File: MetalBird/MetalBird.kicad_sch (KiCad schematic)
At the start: 63 parts, among them J1 Battery Conn, J10 VTX Conn, J2 SWD, J3 ESC1, J4 ESC2, J5 ESC3, J6 ESC4, J7 ELRS Reciver, J8 USB/UART DEBUG, J9 Camera Conn, Q1 PMOS, SW1 SW_Push_Open, U1 STM32F411CEUx, U2 AMS1117-3.3, U3 MPU-6050, U4 BMP280, Y1 8MHz

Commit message: Assign Footprints to components
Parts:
- C1, C10, C11, C12, C13, C15, C16, C17, C18, C1A1, C20, C21, C22, C23, C25, C3, C4, C5, C6, C7, C8, C9: footprint (none) -> Capacitor_SMD:C_0603_1608Metric
- C14, C19, C2, C2A1: footprint (none) -> Capacitor_SMD:C_1206_3216Metric
- C24: footprint (none) -> Capacitor_THT:CP_Radial_D6.3mm_P2.50mm
- D1, D2: footprint (none) -> LED_SMD:LED_0603_1608Metric
- J1, J10, J3, J4, J5, J6, J9: footprint (none) -> Connector_PinHeader_2.54mm:PinHeader_1x03_P2.54mm_Vertical
- J2, J7, J8: footprint (none) -> Connector_PinHeader_2.54mm:PinHeader_1x04_P2.54mm_Vertical
- MP2331H1: footprint (none) -> Package_TO_SOT_SMD:SOT-583-8
- Q1: footprint (none) -> Package_TO_SOT_SMD:SOT-23
- R1, R11, R12, R13, R14, R15, R16, R17, R2, R3, R4, R5, R6, R7, R8: footprint (none) -> Resistor_SMD:R_0603_1608Metric
- SW1: footprint (none) -> Button_Switch_SMD:SW_SPST_PTS645Sx43SMTR92
- Y1: footprint (none) -> Crystal:Crystal_SMD_3225-4Pin_3.2x2.5mm
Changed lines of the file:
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@@
 			)
 		)
-		(property "Footprint" ""
+		(property "Footprint" "Capacitor_SMD:C_1206_3216Metric"
 			(at 37.1348 166.37 0)
 			(effects
@@
 			)
 		)
-		(property "Footprint" ""
+		(property "Footprint" "Capacitor_SMD:C_0603_1608Metric"
 			(at 132.3848 129.54 0)
 			(effects
@@
 			)
 		)
-		(property "Footprint" ""
+		(property "Footprint" "LED_SMD:LED_0603_1608Metric"
 			(at 113.03 110.49 0)
 			(effects
@@
 			)
 		)
-		(property "Footprint" ""
+		(property "Footprint" "Capacitor_SMD:C_0603_1608Metric"
 			(at 160.02 44.1452 0)
 			(effects
@@
 			)
 		)
-		(property "Footprint" ""
+		(property "Footprint" "Connector_PinHeader_2.54mm:PinHeader_1x04_P2.54mm_Vertical"
 			(at 43.18 85.09 0)
 			(effects
@@
 			)
 		)
-		(property "Footprint" ""
+		(property "Footprint" "Capacitor_SMD:C_0603_1608Metric"
 			(at 49.8348 166.37 0)
 			(effects
@@
 			)
 		)
-		(property "Footprint" ""
+		(property "Footprint" "Capacitor_SMD:C_0603_1608Metric"
 			(at 100.0252 40.64 0)
 			(effects
@@
 			)
 		)
-		(property "Footprint" ""
+		(property "Footprint" "Resistor_SMD:R_0603_1608Metric"
 			(at 87.63 171.958 90)
 			(effects
@@
 			)
 		)
-		(property "Footprint" ""
+		(property "Footprint" "Crystal:Crystal_SMD_3225-4Pin_3.2x2.5mm"
 			(at 124.46 63.5 0)
 			(effects
@@
 			)
 		)
-		(property "Footprint" ""
+		(property "Footprint" "Capacitor_SMD:C_1206_3216Metric"
 			(at 134.3152 179.07 0)
 			(effects
@@
 			)
 		)
-		(property "Footprint" ""
+		(property "Footprint" "Connector_PinHeader_2.54mm:PinHeader_1x03_P2.54mm_Vertical"
 			(at 212.09 80.01 0)
 			(effects
@@
 			)
 		)
-		(property "Footprint" ""
+		(property "Footprint" "Capacitor_SMD:C_0603_1608Metric"
 			(at 114.3 73.3552 0)
 			(effects
@@
 			)
 		)
-		(property "Footprint" ""
+		(property "Footprint" "Connector_PinHeader_2.54mm:PinHeader_1x03_P2.54mm_Vertical"
 			(at 43.18 44.45 0)
 			(effects
@@
 			)
 		)
-		(property "Footprint" ""
+		(property "Footprint" "Resistor_SMD:R_0603_1608Metric"
 			(at 120.65 112.268 90)
 			(effects
@@
 			)
 		)
-		(property "Footprint" ""
+		(property "Footprint" "Capacitor_SMD:C_0603_1608Metric"
 			(at 65.0748 151.13 0)
 			(effects
@@
 			)
 		)
-		(property "Footprint" ""
+		(property "Footprint" "Capacitor_SMD:C_0603_1608Metric"
 			(at 111.76 146.3548 0)
 			(effects
@@
 			)
 		)
-		(property "Footprint" ""
+		(property "Footprint" "Resistor_SMD:R_0603_1608Metric"
 			(at 29.972 41.91 90)
 			(effects
@@
 			)
 		)
-		(property "Footprint" ""
+		(property "Footprint" "Connector_PinHeader_2.54mm:PinHeader_1x03_P2.54mm_Vertical"
 			(at 212.09 95.25 0)
 			(effects
@@
 			)
 		)
-		(property "Footprint" ""
+		(property "Footprint" "Capacitor_SMD:C_0603_1608Metric"
 			(at 195.2752 62.23 0)
 			(effects
@@
 			)
 		)
-		(property "Footprint" ""
+		(property "Footprint" "Capacitor_SMD:C_0603_1608Metric"
 			(at 294.64 89.2048 0)
 			(effects
@@
 			)
 		)
-		(property "Footprint" ""
+		(property "Footprint" "Capacitor_SMD:C_0603_1608Metric"
 			(at 122.8852 40.64 0)
 			(effects
@@
 			)
 		)
-		(property "Footprint" ""
+		(property "Footprint" "Package_TO_SOT_SMD:SOT-23"
 			(at 29.21 26.67 0)
 			(effects
@@
 			)
 		)
-		(property "Footprint" ""
+		(property "Footprint" "Capacitor_SMD:C_0603_1608Metric"
 			(at 274.6248 139.7 0)
 			(effects
@@
 			)
 		)
-		(property "Footprint" ""
+		(property "Footprint" "LED_SMD:LED_0603_1608Metric"
 			(at 113.03 116.84 0)
 			(effects
@@
 			)
 		)
-		(property "Footprint" ""
+		(property "Footprint" "Connector_PinHeader_2.54mm:PinHeader_1x04_P2.54mm_Vertical"
 			(at 43.18 66.04 0)
 			(effects
@@
 			)
 		)
-		(property "Footprint" ""
+		(property "Footprint" "Resistor_SMD:R_0603_1608Metric"
 			(at 188.722 49.53 90)
 			(effects
@@
 			)
 		)
-		(property "Footprint" ""
+		(property "Footprint" "Capacitor_SMD:C_1206_3216Metric"
 			(at 192.7352 179.07 0)
 			(effects
@@
 			)
 		)
-		(property "Footprint" ""
+		(property "Footprint" "Capacitor_SMD:C_0603_1608Metric"
 			(at 114.3 65.0748 0)
 			(effects
@@
 			)
 		)
-		(property "Footprint" ""
+		(property "Footprint" "Capacitor_SMD:C_0603_1608Metric"
 			(at 265.1252 60.96 0)
 			(effects
@@
 			)
 		)
-		(property "Footprint" ""
+		(property "Footprint" "Capacitor_SMD:C_0603_1608Metric"
 			(at 100.33 169.2148 0)
 			(effects
@@
 			)
 		)
-		(property "Footprint" ""
+		(property "Footprint" "Connector_PinHeader_2.54mm:PinHeader_1x03_P2.54mm_Vertical"
 			(at 43.18 128.27 0)
 			(effects
@@
 			)
 		)
-		(property "Footprint" ""
+		(property "Footprint" "Capacitor_SMD:C_0603_1608Metric"
 			(at 269.5448 139.7 0)
 			(effects
@@
 			)
 		)
-		(property "Footprint" ""
+		(property "Footprint" "Capacitor_SMD:C_0603_1608Metric"
 			(at 76.5048 148.59 0)
 			(effects
@@
 			)
 		)
-		(property "Footprint" ""
+		(property "Footprint" "Button_Switch_SMD:SW_SPST_PTS645Sx43SMTR92"
 			(at 125.73 46.99 0)
 			(effects
@@
 			)
 		)
-		(property "Footprint" ""
+		(property "Footprint" "Connector_PinHeader_2.54mm:PinHeader_1x03_P2.54mm_Vertical"
 			(at 212.09 64.77 0)
 			(effects
@@
 			)
 		)
-		(property "Footprint" ""
+		(property "Footprint" "Resistor_SMD:R_0603_1608Metric"
 			(at 106.68 99.568 90)
 			(effects
@@
 			)
 		)
-		(property "Footprint" ""
+		(property "Footprint" "Resistor_SMD:R_0603_1608Metric"
 			(at 105.41 95.758 90)
 			(effects
@@
 			)
 		)
-		(property "Footprint" ""
+		(property "Footprint" "Package_TO_SOT_SMD:SOT-583-8"
 			(at 73.66 166.37 0)
 			(effects
@@
 			)
 		)
-		(property "Footprint" ""
+		(property "Footprint" "Resistor_SMD:R_0603_1608Metric"
 			(at 192.278 59.69 90)
 			(effects
@@
 			)
 		)
-		(property "Footprint" ""
+		(property "Footprint" "Capacitor_SMD:C_0603_1608Metric"
 			(at 110.1852 40.64 0)
 			(effects
@@
 			)
 		)
-		(property "Footprint" ""
+		(property "Footprint" "Resistor_SMD:R_0603_1608Metric"
 			(at 120.65 115.062 90)
 			(effects
@@
 			)
 		)
-		(property "Footprint" ""
+		(property "Footprint" "Resistor_SMD:R_0603_1608Metric"
 			(at 92.202 152.4 90)
 			(effects
@@
 			)
 		)
-		(property "Footprint" ""
+		(property "Footprint" "Resistor_SMD:R_0603_1608Metric"
 			(at 116.84 58.928 90)
 			(effects
@@
 			)
 		)
-		(property "Footprint" ""
+		(property "Footprint" "Capacitor_THT:CP_Radial_D6.3mm_P2.50mm"
 			(at 26.3652 52.07 0)
 			(effects
@@
 			)
 		)
-		(property "Footprint" ""
+		(property "Footprint" "Connector_PinHeader_2.54mm:PinHeader_1x03_P2.54mm_Vertical"
 			(at 43.18 116.84 0)
 			(effects
@@
 			)
 		)
-		(property "Footprint" ""
+		(property "Footprint" "Resistor_SMD:R_0603_1608Metric"
 			(at 27.178 175.26 90)
 			(effects
@@
 			)
 		)
-		(property "Footprint" ""
+		(property "Footprint" "Resistor_SMD:R_0603_1608Metric"
 			(at 88.9 163.068 90)
 			(effects
@@
 			)
 		)
-		(property "Footprint" ""
+		(property "Footprint" "Capacitor_SMD:C_0603_1608Metric"
 			(at 288.29 91.7448 0)
 			(effects
@@
 			)
 		)
-		(property "Footprint" ""
+		(property "Footprint" "Capacitor_SMD:C_0603_1608Metric"
 			(at 89.8652 40.64 0)
 			(effects
@@
 			)
 		)
-		(property "Footprint" ""
+		(property "Footprint" "Resistor_SMD:R_0603_1608Metric"
 			(at 107.95 155.702 90)
 			(effects
@@
 			)
 		)
-		(property "Footprint" ""
+		(property "Footprint" "Resistor_SMD:R_0603_1608Metric"
 			(at 132.842 43.18 90)
 			(effects
@@
 			)
 		)
-		(property "Footprint" ""
+		(property "Footprint" "Capacitor_SMD:C_1206_3216Metric"
 			(at 124.1552 179.07 0)
 			(effects
@@
 			)
 		)
-		(property "Footprint" ""
+		(property "Footprint" "Capacitor_SMD:C_0603_1608Metric"
 			(at 166.0652 177.8 0)
 			(effects
@@
 			)
 		)
-		(property "Footprint" ""
+		(property "Footprint" "Connector_PinHeader_2.54mm:PinHeader_1x03_P2.54mm_Vertical"
 			(at 212.09 110.49 0)
 			(effects
@@
 			)
 		)
-		(property "Footprint" ""
+		(property "Footprint" "Capacitor_SMD:C_0603_1608Metric"
 			(at 258.1148 60.96 0)
 			(effects
@@
 			)
 		)
-		(property "Footprint" ""
+		(property "Footprint" "Connector_PinHeader_2.54mm:PinHeader_1x04_P2.54mm_Vertical"
 			(at 43.18 100.33 0)
 			(effects
@@
 			)
 		)
-		(property "Footprint" ""
+		(property "Footprint" "Resistor_SMD:R_0603_1608Metric"
 			(at 107.95 103.378 90)
 			(effects
@@
 			)
 		)
-		(property "Footprint" ""
+		(property "Footprint" "Capacitor_SMD:C_0603_1608Metric"
 			(at 79.7052 40.64 0)
 			(effects

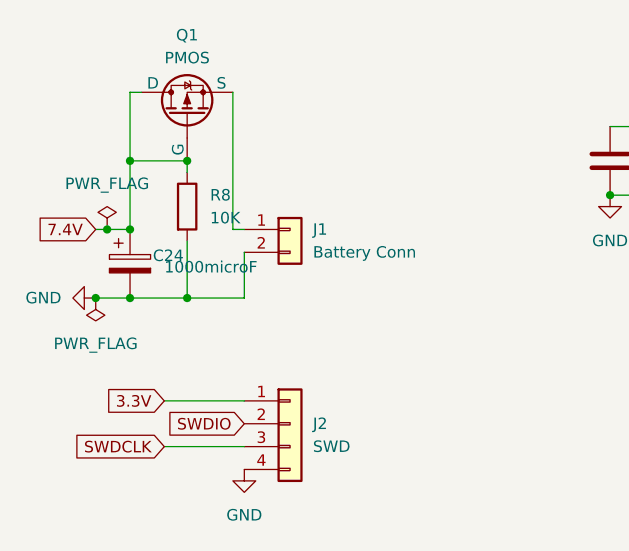
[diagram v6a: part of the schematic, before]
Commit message: PCB Design
laid out all the components in 36x36mm board
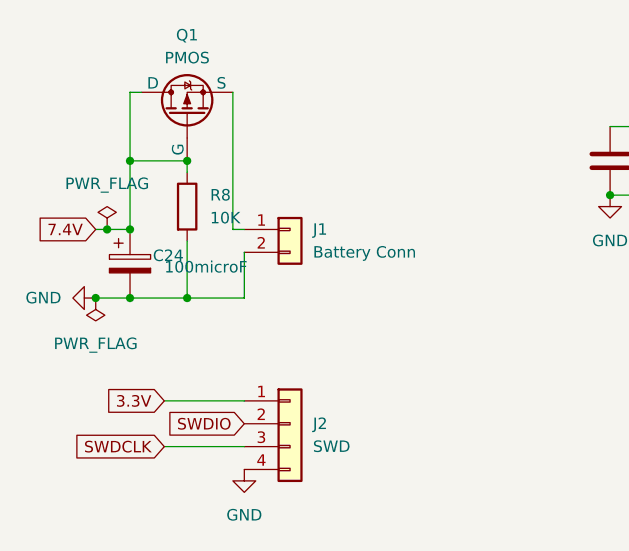
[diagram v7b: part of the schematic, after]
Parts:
- C24: value 1000microF -> 100microF; footprint Capacitor_THT:CP_Radial_D6.3mm_P2.50mm -> Capacitor_SMD:C_1206_3216Metric
- L1: footprint (none) -> Inductor_SMD:L_Cenker_CKCS4018
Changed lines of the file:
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@@
 			)
 		)
-		(property "Footprint" ""
+		(property "Footprint" "Inductor_SMD:L_Cenker_CKCS4018"
 			(at 105.41 170.18 0)
 			(effects
@@
 			)
 		)
-		(property "Value" "1000microF"
+		(property "Value" "100microF"
 			(at 29.21 48.6409 0)
 			(effects
@@
 			)
 		)
-		(property "Footprint" "Capacitor_THT:CP_Radial_D6.3mm_P2.50mm"
+		(property "Footprint" "Capacitor_SMD:C_1206_3216Metric"
 			(at 26.3652 52.07 0)
 			(effects

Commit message: Routing Complete
- yet to fix cosmetic stuff (silk overlap)
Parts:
- J1: footprint Connector_PinHeader_2.54mm:PinHeader_1x03_P2.54mm_Vertical -> Connector_JST:JST_PH_B2B-PH-K_1x02_P2.00mm_Vertical
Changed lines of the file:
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@@
 			)
 		)
-		(property "Footprint" "Connector_PinHeader_2.54mm:PinHeader_1x03_P2.54mm_Vertical"
+		(property "Footprint" "Connector_JST:JST_PH_B2B-PH-K_1x02_P2.00mm_Vertical"
 			(at 43.18 44.45 0)
 			(effects
